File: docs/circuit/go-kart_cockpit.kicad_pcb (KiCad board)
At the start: 2 copper layers, 103.5 x 57.2 mm, 36 parts, among them P1 Power, Q1 TIP120, X1 Taster rechts (male), X10 Display (male), X11 PD7, X14 AVR-ISP-10, X15 Taster links (male), X16 Start/Stop/Rückwärts, X17 SDA PG4, X2 5V GND, X3 24V Hupe, X4 SCL, X5 CS, X6 PB6, X7 J5, X8 J3, X9 Bluetooth-Modul

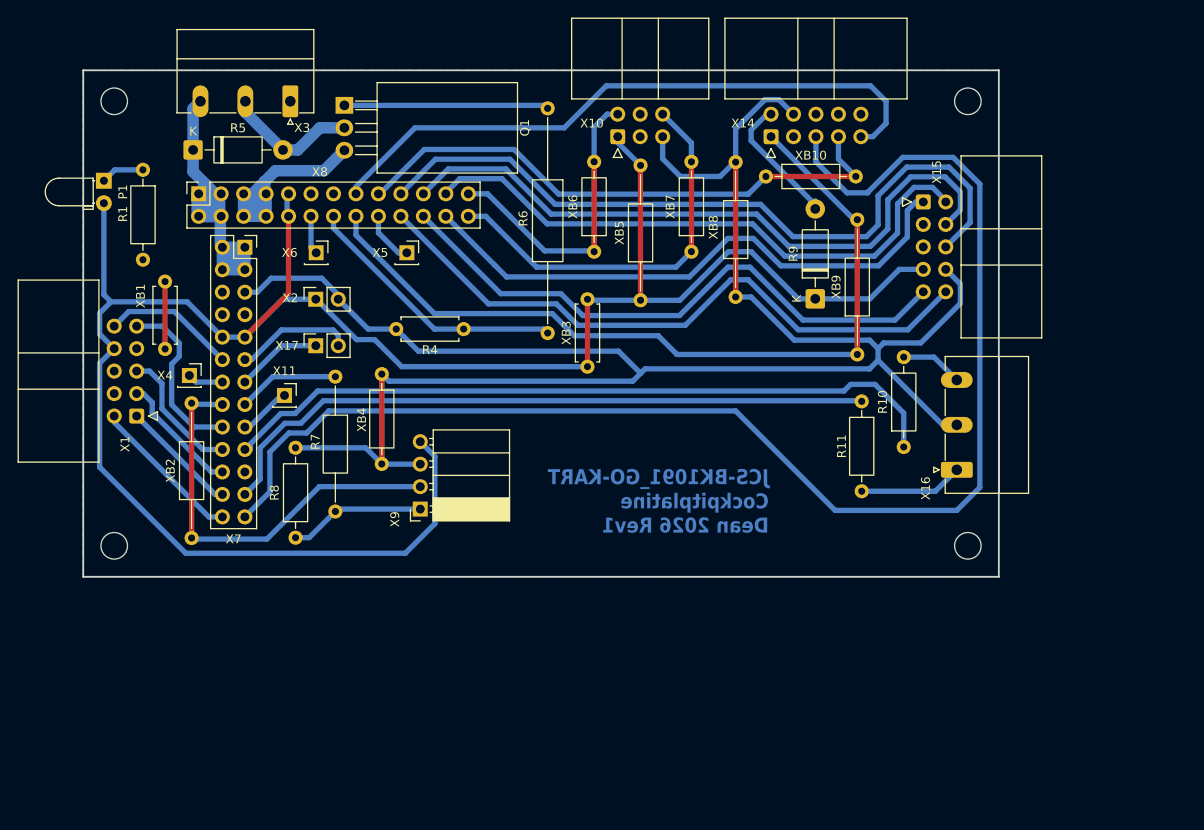
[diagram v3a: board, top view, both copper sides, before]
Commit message: feat(PCB): replace TIP120 with MOSFET
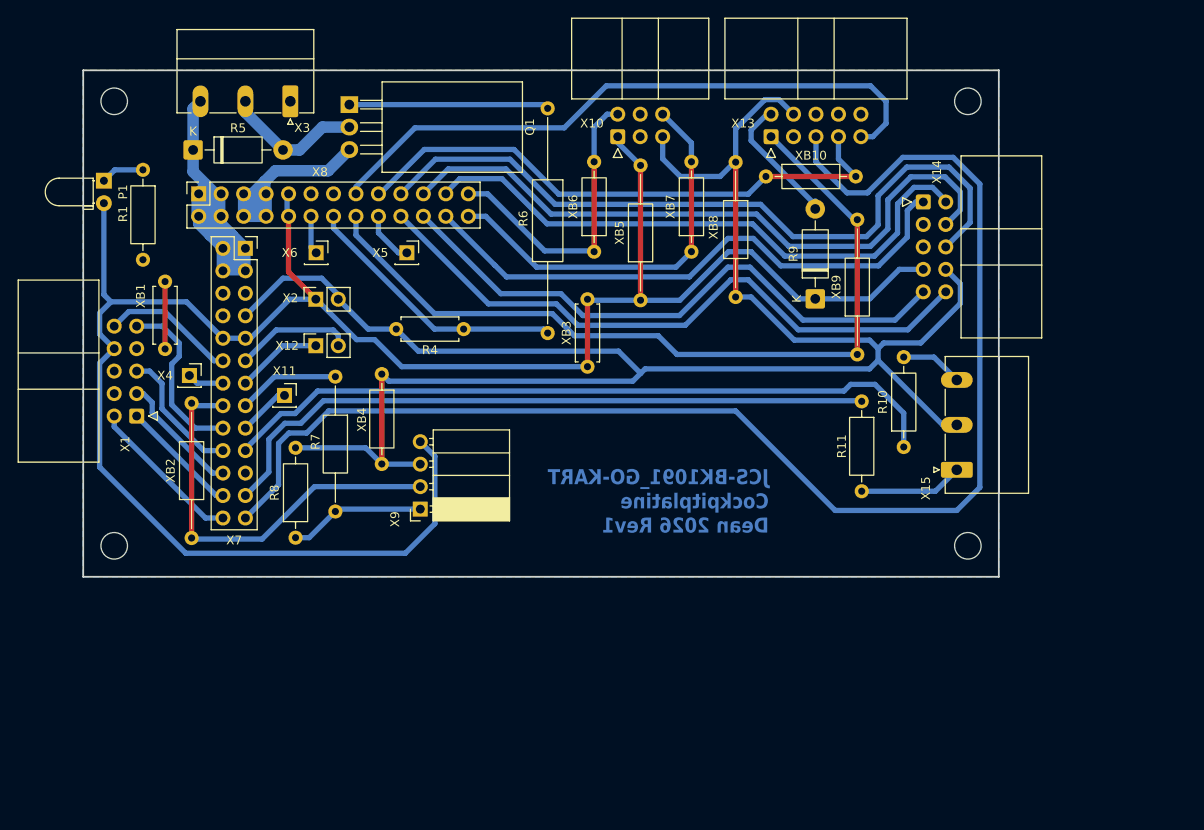
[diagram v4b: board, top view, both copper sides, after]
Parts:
- Q1: value TIP120 -> IRLIZ44N
- R6: value 470 -> 100
- moved Q1 0.57 mm to (69.2, 32.0)
- moved X7 0.14 mm to (57.5, 48.2)
- renumbered X17 to X12, X14 to X13, X15 to X14, X16 to X15
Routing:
- net +24V: track 54.1 -> 69.4 mm
- net Vcc (5V): track 236.5 -> 231.5 mm
- net GND: track 260.2 -> 261.8 mm
- net Net-(Q1-G): track 23.3 -> 22.6 mm
- net /Hupe (-): track 15.2 -> 15.8 mm
- net /PD7: track 5.96 -> 6.49 mm

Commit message: feat: rework of PCB, fix wrong connection
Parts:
- removed R10: 100, Resistor_THT:R_Axial_DIN0207_L6.3mm_D2.5mm_P10.16mm_Horizontal
- removed the R7 at (67.7, 62.8)
- removed R8: 5.6k, Resistor_THT:R_Axial_DIN0207_L6.3mm_D2.5mm_P10.16mm_Horizontal
- removed the X11 at (61.9, 64.9)
- removed the X2 at (65.5, 54.0)
- removed the X6 at (65.5, 48.8)
- added R2: 100, Resistor_THT:R_Axial_DIN0207_L6.3mm_D2.5mm_P10.16mm_Horizontal, F.Cu at (71.8, 59.5)
- added R3: 820, Resistor_THT:R_Axial_DIN0309_L9.0mm_D3.2mm_P12.70mm_Horizontal, F.Cu at (121.0, 44.9)
- added R5: 5.6k, Resistor_THT:R_Axial_DIN0207_L6.3mm_D2.5mm_P10.16mm_Horizontal, F.Cu at (79.2, 95.2)
- added X10: CS, Connector_PinSocket_2.54mm:PinSocket_1x01_P2.54mm_Vertical, F.Cu at (76.2, 70.2)
- added X7: PD1 PG4 VCC GND, Connector_PinSocket_2.54mm:PinSocket_1x04_P2.54mm_Vertical, F.Cu at (62.2, 85.4)
- added XB11: MISO, TestPoint:TestPoint_2Pads_Pitch5.08mm_Drill1.3mm, F.Cu at (127.2, 100.1)
- added XB12: /RESET, Resistor_THT:R_Axial_DIN0207_L6.3mm_D2.5mm_P15.24mm_Horizontal, F.Cu at (95.6, 95.0)
- Q1: value IRLIZ44N -> IRL3803; footprint Library:TO-220-3_Horizontal_TabDown_no_hole -> Package_TO_SOT_THT:TO-220F-3_Horizontal_TabDown
- R1: value 820 -> 100
- R11: value 100 -> 10k; footprint Resistor_THT:R_Axial_DIN0207_L6.3mm_D2.5mm_P10.16mm_Horizontal -> Resistor_THT:R_Axial_DIN0207_L6.3mm_D2.5mm_P7.62mm_Horizontal
- R4: value 10k -> 3.3k; footprint Resistor_THT:R_Axial_DIN0207_L6.3mm_D2.5mm_P7.62mm_Horizontal -> Resistor_THT:R_Axial_DIN0207_L6.3mm_D2.5mm_P10.16mm_Horizontal
- R6: value 100 -> 1N5817; footprint Resistor_THT:R_Axial_DIN0309_L9.0mm_D3.2mm_P25.40mm_Horizontal -> Diode_THT:D_DO-41_SOD81_P10.16mm_Horizontal
- R9: value 1N5817 -> 100; footprint Diode_THT:D_DO-41_SOD81_P10.16mm_Horizontal -> Resistor_THT:R_Axial_DIN0207_L6.3mm_D2.5mm_P7.62mm_Horizontal
- X12: value SDA PG4 -> PB6; footprint Connector_PinSocket_2.54mm:PinSocket_1x02_P2.54mm_Vertical -> Connector_PinSocket_2.54mm:PinSocket_1x01_P2.54mm_Vertical
- X4: value SCL -> PC2 PG1 PD7; footprint Connector_PinSocket_2.54mm:PinSocket_1x01_P2.54mm_Vertical -> Connector_PinSocket_2.54mm:PinSocket_1x03_P2.54mm_Vertical
- X5: value CS -> SCL
- XB1: footprint Resistor_THT:R_Axial_DIN0207_L6.3mm_D2.5mm_P7.62mm_Horizontal -> Resistor_THT:R_Axial_DIN0207_L6.3mm_D2.5mm_P10.16mm_Horizontal
- XB10: value ISP_SCK -> TXD0
- XB2: value ~ -> Vcc; footprint Resistor_THT:R_Axial_DIN0207_L6.3mm_D2.5mm_P15.24mm_Horizontal -> Resistor_THT:R_Axial_DIN0207_L6.3mm_D2.5mm_P10.16mm_Horizontal
- XB3: value Display_Vcc -> Vcc; footprint Resistor_THT:R_Axial_DIN0207_L6.3mm_D2.5mm_P7.62mm_Horizontal -> Resistor_THT:R_Axial_DIN0207_L6.3mm_D2.5mm_P10.16mm_Horizontal
- XB4: value Display_GND -> Vcc; footprint Resistor_THT:R_Axial_DIN0207_L6.3mm_D2.5mm_P10.16mm_Horizontal -> Resistor_THT:R_Axial_DIN0207_L6.3mm_D2.5mm_P7.62mm_Horizontal
- XB5: value Display_Vcc -> GND
- XB6: value TXD0 -> GND
- XB7: value RXD0 -> GND; footprint Resistor_THT:R_Axial_DIN0207_L6.3mm_D2.5mm_P10.16mm_Horizontal -> Resistor_THT:R_Axial_DIN0207_L6.3mm_D2.5mm_P7.62mm_Horizontal
- XB8: value GND -> ~
- XB9: value ISP_MOSI -> RXD0; footprint Resistor_THT:R_Axial_DIN0207_L6.3mm_D2.5mm_P15.24mm_Horizontal -> Resistor_THT:R_Axial_DIN0207_L6.3mm_D2.5mm_P10.16mm_Horizontal
- moved XB8 89.0 mm to (52.5, 103.9), turned to 90 degrees
- moved P1 85.5 mm to (126.8, 46.6), turned to 180 degrees
- moved X14 79.3 mm to (95.3, 103.9), turned to 0 degrees
- moved R7 75.7 mm to (95.4, 98.9)
- moved Q1 74.8 mm to (122.3, 84.8), turned to 180 degrees
- moved X1 73.8 mm to (69.5, 45.4), turned to 180 degrees
- moved R11 55.7 mm to (72.1, 73.5), turned to 180 degrees
- moved XB4 53.5 mm to (126.2, 58.0), turned to 90 degrees
- moved R6 43.9 mm to (124.2, 61.9)
- moved X13 43.4 mm to (129.2, 77.2), turned to 0 degrees
- moved X5 42.6 mm to (52.2, 84.2)
- moved R4 41.2 mm to (66.0, 95.2), turned to 0 degrees
- moved X2 39.5 mm to (81.4, 51.3), turned to 90 degrees
- moved X9 38.6 mm to (129.2, 60.4), turned to 0 degrees
- moved X4 36.0 mm to (62.2, 96.8), turned to 180 degrees
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- renumbered R5 to R7, X15 to X1, X8 to X11, X3 to X14, X1 to X2, X14 to X3, X7 to X6, X9 to X8, X10 to X9
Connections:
- R1 pad 1: Net-(P1-K) -> /PB7_SW_Reverse
- R1 pad 2: GND -> Net-(X1-4)
- R11 pad 1: /PC2_SW_Start -> PB4_OC2A
- R11 pad 2: Net-(R11-Pad2) -> GND
- R4 pad 1: PB4_OC2A -> PD3_TXD1
- R4 pad 2: GND -> /BL_RX3V3
- R6 pad 1: Net-(Q1-G) -> Vcc (5V)
- R6 pad 2: PB4_OC2A -> Net-(R6-A)
- R9 pad 1: Vcc (5V) -> Net-(Q1-G)
- R9 pad 2: Net-(R9-A) -> PB4_OC2A
- X1 pad 1: Net-(R11-Pad2) -> Net-(R2-Pad2)
- X1 pad 3: Net-(X15-4) -> Net-(X1-4)
- X11 pad 11: unconnected-(X8-Pin_11-Pad11) -> /PB7_SW_Reverse
- X11 pad 13: unconnected-(X8-Pin_13-Pad13) -> /PB5_SW_Start
- X12 pad 1: /PD1_SDA -> /PB6_OC1B
- X13 pad 2: Net-(R9-A) -> Net-(R6-A)
- X14 pad 2: /Hupe (-) -> +24V
- X14 pad 3: +24V -> /Hupe (-)
- X4 pad 1: /PD0_SCL -> /PC2
- X5 pad 1: /PB0_CS -> /PD0_SCL
- X6 pad 19: /PG1_SW_Reverse -> /PG1
- X6 pad 23: /PC2_SW_Start -> /PC2
- X9 pad 2: PE1_TXD0 -> PE0_RXD0
- X9 pad 6: PE0_RXD0 -> PE1_TXD0
- XB10 pad 1: PB1_SCK -> PE1_TXD0
- XB10 pad 2: PB1_SCK -> PE1_TXD0
- XB2 pad 1: PD2_RXD1 -> Vcc (5V)
- XB2 pad 2: PD2_RXD1 -> Vcc (5V)
- XB4 pad 1: GND -> Vcc (5V)
- XB4 pad 2: GND -> Vcc (5V)
- XB5 pad 1: Vcc (5V) -> GND
- XB5 pad 2: Vcc (5V) -> GND
- XB6 pad 1: PE1_TXD0 -> GND
- XB6 pad 2: PE1_TXD0 -> GND
- XB7 pad 1: PE0_RXD0 -> GND
- XB7 pad 2: PE0_RXD0 -> GND
- XB8 pad 1: GND -> PD2_RXD1
- XB8 pad 2: GND -> PD2_RXD1
- XB9 pad 1: PB2_MOSI -> PE0_RXD0
- XB9 pad 2: PB2_MOSI -> PE0_RXD0
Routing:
- net /PG1_SW_Reverse: track 84.1 -> 0.00 mm
- net /PC2_SW_Start: track 76.3 -> 0.00 mm
- net PB1_SCK: track 64.3 -> 138.4 mm
- net PC0_SW_BlinkerR: track 13.5 -> 84.5 mm
- net PB3_MISO: track 72.1 -> 143.0 mm
- net PC3_LED_BlinkerR: track 17.8 -> 88.4 mm
- net PG2_SW_GearDown: track 14.2 -> 81.4 mm
- net PG0_SW_GearUp: track 15.1 -> 79.3 mm
- net PD4_LED_GearUp: track 19.8 -> 83.5 mm
- net PG3_LED_GearDown: track 15.3 -> 77.3 mm
- net +24V: track 69.4 -> 129.9 mm
- net Vcc (5V): track 231.5 -> 179.9 mm
- net GND: track 261.8 -> 305.9 mm
- net /RESET: track 156.6 -> 116.1 mm
- net PE7_SW_Warnblinker: track 83.5 -> 46.4 mm
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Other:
- board size 103.5 x 57.2 mm -> 96.8 x 66.2 mm
- board text added: "DSUB9-CAN"
- board text added: "JCS-BK1091_GO-KART Cockpitplatine Dean 2026 Rev2"
- board text added: "M2"
- board text removed: "JCS-BK1091_GO-KART Cockpitplatine Dean 2026 Rev1"

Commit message: feat(PCB): replace 100 ohm preresistors with 330
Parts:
- R1, R2: value 100 -> 330
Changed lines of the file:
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@@
 			)
 		)
-		(property "Value" "100"
+		(property "Value" "330"
 			(at 5.08 2.37 90)
 			(layer "F.Fab")
@@
 			)
 		)
-		(property "Value" "100"
+		(property "Value" "330"
 			(at 5.08 2.37 90)
 			(layer "F.Fab")
@@
 	)
 	(zone
-		(net 38)
-		(net_name "{slash}PB5_SW_Start")
-		(layer "B.Cu")
-		(name "$teardrop_padvia$")
-		(hatch none 0.1)
-		(priority 30125)
-		(attr
-			(teardrop
-				(type padvia)
-			)
-		)
-		(connect_pads yes
-			(clearance 0)
-		)
-		(min_thickness 0.0254)
-		(filled_areas_thickness no)
-		(fill yes
-			(thermal_gap 0.5)
-			(thermal_bridge_width 0.5)
-			(island_removal_mode 1)
-			(island_area_min 10)
-		)
-		(polygon
-			(pts
-				(xy 70.277304 60.548432) (xy 70.701568 60.972696) (xy 72.250013 60.248323) (xy 71.750707 59.499293)
-				(xy 71.001677 58.999987)
-			)
-		)
-	)
-	(zone
 		(net 11)
 		(net_name "{slash}RESET")
@@
 	)
 	(zone
-		(net 40)
-		(net_name "Net-(X1-4)")
-		(layer "B.Cu")
-		(name "$teardrop_padvia$")
-		(hatch none 0.1)
-		(priority 30140)
-		(attr
-			(teardrop
-				(type padvia)
-			)
-		)
-		(connect_pads yes
-			(clearance 0)
-		)
-		(min_thickness 0.0254)
-		(filled_areas_thickness no)
-		(fill yes
-			(thermal_gap 0.5)
-			(thermal_bridge_width 0.5)
-			(island_removal_mode 1)
-			(island_area_min 10)
-		)
-		(polygon
-			(pts
-				(xy 58.60693 48.067334) (xy 58.182666 47.64307) (xy 56.999987 48.591677) (xy 57.499293 49.340707)
-				(xy 58.382707 49.515581)
-			)
-		)
-	)
-	(zone
 		(net 4)
 		(net_name "+24V")
@@
 	)
 	(zone
+		(net 41)
+		(net_name "Net-(R2-Pad2)")
+		(layer "B.Cu")
+		(name "$teardrop_padvia$")
+		(hatch none 0.1)
+		(priority 30004)
+		(attr
+			(teardrop
+				(type padvia)
+			)
+		)
+		(connect_pads yes
+			(clearance 0)
+		)
+		(min_thickness 0.0254)
+		(filled_areas_thickness no)
+		(fill yes
+			(thermal_gap 0.5)
+			(thermal_bridge_width 0.5)
+			(island_removal_mode 1)
+			(island_area_min 10)
+		)
+		(polygon
+			(pts
+				(xy 71.067334 47.64307) (xy 70.64307 48.067334) (xy 70.867293 49.515581) (xy 71.750707 49.340707)
+				(xy 72.250013 48.591677)
+			)
+		)
+	)
+	(zone
 		(net 22)
 		(net_name "PE3_SW_BlinkerL")
@@
 	)
 	(zone
-		(net 4)
-		(net_name "+24V")
+		(net 1)
+		(net_name "/Hupe (-)")
 		(layer "B.Cu")
 		(name "$teardrop_padvia$")
 		(hatch none 0.1)
-		(priority 30033)
+		(priority 30000)
 		(attr
 			(teardrop
@@
 		(polygon
 			(pts
-				(xy 55.239056 68.406909) (xy 54.319817 69.326148) (xy 55.291677 70.627105) (xy 56.040707 70.127799)
-				(xy 56.540013 69.378769)
+				(xy 119.1 86.704198) (xy 120.4 86.704198) (xy 120.684198 85.003324) (xy 119.75 84.769) (xy 118.815802 85.003324)
 			)
 		)
 	)
 	(zone
-		(net 37)
-		(net_name "{slash}PB7_SW_Reverse")
+		(net 4)
+		(net_name "+24V")
 		(layer "B.Cu")
 		(name "$teardrop_padvia$")
 		(hatch none 0.1)
-		(priority 30129)
+		(priority 30033)
 		(attr
 			(teardrop
@@
 		(polygon
 			(pts
-				(xy 58.972696 58.451568) (xy 58.548432 58.027304) (xy 56.999987 58.751677) (xy 57.499293 59.500707)
-				(xy 58.248323 60.000013)
+				(xy 55.239056 68.406909) (xy 54.319817 69.326148) (xy 55.291677 70.627105) (xy 56.040707 70.127799)
+				(xy 56.540013 69.378769)
 			)
 		)
@@
 	)
 	(zone
+		(net 40)
+		(net_name "Net-(X1-4)")
+		(layer "B.Cu")
+		(name "$teardrop_padvia$")
+		(hatch none 0.1)
+		(priority 30003)
+		(attr
+			(teardrop
+				(type padvia)
+			)
+		)
+		(connect_pads yes
+			(clearance 0)
+		)
+		(min_thickness 0.0254)
+		(filled_areas_thickness no)
+		(fill yes
+			(thermal_gap 0.5)
+			(thermal_bridge_width 0.5)
+			(island_removal_mode 1)
+			(island_area_min 10)
+		)
+		(polygon
+			(pts
+				(xy 58.60693 48.067334) (xy 58.182666 47.64307) (xy 56.999987 48.591677) (xy 57.499293 49.340707)
+				(xy 58.382707 49.515581)
+			)
+		)
+	)
+	(zone
 		(net 31)
 		(net_name "/PB6_OC1B")
@@
 	)
 	(zone
-		(net 3)
-		(net_name "Net-(Q1-G)")
+		(net 5)
+		(net_name "Vcc (5V)")
 		(layer "B.Cu")
 		(name "$teardrop_padvia$")
 		(hatch none 0.1)
-		(priority 30144)
+		(priority 30137)
 		(attr
 			(teardrop
@@
 		(polygon
 			(pts
-				(xy 121.906309 82.732045) (xy 121.482045 83.156309) (xy 121.3375 83.77) (xy 122.290707 84.770707)
-				(xy 122.965895 83.77)
+				(xy 127.971091 59.296828) (xy 127.546828 59.721091) (xy 128.36 60.890163) (xy 129.210707 60.420707)
+				(xy 129.454361 59.57)
 			)
 		)
 	)
 	(zone
-		(net 5)
-		(net_name "Vcc (5V)")
+		(net 14)
+		(net_name "/PD1_SDA")
 		(layer "B.Cu")
 		(name "$teardrop_padvia$")
 		(hatch none 0.1)
-		(priority 30137)
+		(priority 30065)
 		(attr
 			(teardrop
@@
 		(polygon
 			(pts
-				(xy 127.971091 59.296828) (xy 127.546828 59.721091) (xy 128.36 60.890163) (xy 129.210707 60.420707)
-				(xy 129.454361 59.57)
+				(xy 60.25 85.067092) (xy 60.25 85.667092) (xy 61.25 86.368546) (xy 62.251 85.37) (xy 61.25 84.37)
 			)
 		)
 	)
 	(zone
-		(net 14)
-		(net_name "/PD1_SDA")
+		(net 9)
+		(net_name "PE0_RXD0")
 		(layer "B.Cu")
 		(name "$teardrop_padvia$")
 		(hatch none 0.1)
-		(priority 30065)
+		(priority 30136)
 		(attr
 			(teardrop
@@
 		(polygon
 			(pts
-				(xy 60.25 85.067092) (xy 60.25 85.667092) (xy 61.25 86.368546) (xy 62.251 85.37) (xy 61.25 84.37)
+				(xy 132.7284 61.822664) (xy 133.152664 61.3984) (xy 132.456749 59.947765) (xy 131.749293 60.419293)
+				(xy 131.277765 61.126749)
 			)
 		)
 	)
 	(zone
-		(net 9)
-		(net_name "PE0_RXD0")
+		(net 32)
+		(net_name "/PD7")
 		(layer "B.Cu")
 		(name "$teardrop_padvia$")
 		(hatch none 0.1)
-		(priority 30136)
+		(priority 30145)
 		(attr
 			(teardrop
@@
 		(polygon
 			(pts
-				(xy 132.7284 61.822664) (xy 133.152664 61.3984) (xy 132.456749 59.947765) (xy 131.749293 60.419293)
-				(xy 131.277765 61.126749)
+				(xy 60.028844 90.953108) (xy 60.453108 90.528844) (xy 59.080013 89.698769) (xy 58.579293 90.446385)
+				(xy 58.755581 91.329799)
 			)
 		)
 	)
 	(zone
-		(net 32)
-		(net_name "/PD7")
+		(net 37)
+		(net_name "{slash}PB7_SW_Reverse")
 		(layer "B.Cu")
 		(name "$teardrop_padvia$")
 		(hatch none 0.1)
-		(priority 30145)
+		(priority 30001)
 		(attr
 			(teardrop
@@
 		(polygon
 			(pts
-				(xy 60.028844 90.953108) (xy 60.453108 90.528844) (xy 59.080013 89.698769) (xy 58.579293 90.446385)
-				(xy 58.755581 91.329799)
+				(xy 58.972696 58.451568) (xy 58.548432 58.027304) (xy 56.999987 58.751677) (xy 57.499293 59.500707)
+				(xy 58.248323 60.000013)
 			)
 		)
@@
 	)
 	(zone
+		(net 3)
+		(net_name "Net-(Q1-G)")
+		(layer "B.Cu")
+		(name "$teardrop_padvia$")
+		(hatch none 0.1)
+		(priority 30005)
+		(attr
+			(teardrop
+				(type padvia)
+			)
+		)
+		(connect_pads yes
+			(clearance 0)
+		)
+		(min_thickness 0.0254)
+		(filled_areas_thickness no)
+		(fill yes
+			(thermal_gap 0.5)
+			(thermal_bridge_width 0.5)
+			(island_removal_mode 1)
+			(island_area_min 10)
+		)
+		(polygon
+			(pts
+				(xy 121.906309 82.732045) (xy 121.482045 83.156309) (xy 121.3375 83.77) (xy 122.290707 84.770707)
+				(xy 122.965895 83.77)
+			)
+		)
+	)
+	(zone
 		(net 6)
 		(net_name "PD3_TXD1")
@@
 	)
 	(zone
+		(net 38)
+		(net_name "{slash}PB5_SW_Start")
+		(layer "B.Cu")
+		(name "$teardrop_padvia$")
+		(hatch none 0.1)
+		(priority 30002)
+		(attr
+			(teardrop
+				(type padvia)
+			)
+		)
+		(connect_pads yes
+			(clearance 0)
+		)
+		(min_thickness 0.0254)
+		(filled_areas_thickness no)
+		(fill yes
+			(thermal_gap 0.5)
+			(thermal_bridge_width 0.5)
+			(island_removal_mode 1)
+			(island_area_min 10)
+		)
+		(polygon
+			(pts
+				(xy 70.277304 60.548432) (xy 70.701568 60.972696) (xy 72.250013 60.248323) (xy 71.750707 59.499293)
+				(xy 71.001677 58.999987)
+			)
+		)
+	)
+	(zone
 		(net 4)
 		(net_name "+24V")
@@
 	)
 	(zone
-		(net 1)
-		(net_name "/Hupe (-)")
-		(layer "B.Cu")
-		(name "$teardrop_padvia$")
-		(hatch none 0.1)
-		(priority 30011)
-		(attr
-			(teardrop
-				(type padvia)
-			)
-		)
-		(connect_pads yes
-			(clearance 0)
-		)
-		(min_thickness 0.0254)
-		(filled_areas_thickness no)
-		(fill yes
-			(thermal_gap 0.5)
-			(thermal_bridge_width 0.5)
-			(island_removal_mode 1)
-			(island_area_min 10)
-		)
-		(polygon
-			(pts
-				(xy 119.1 86.704198) (xy 120.4 86.704198) (xy 120.684198 85.003324) (xy 119.75 84.769) (xy 118.815802 85.003324)
-			)
-		)
-	)
-	(zone
 		(net 9)
 		(net_name "PE0_RXD0")
@@
 			)
 		)
-	)
-	(zone
-		(net 41)
-		(net_name "Net-(R2-Pad2)")
-		(layer "B.Cu")
-		(name "$teardrop_padvia$")
-		(hatch none 0.1)
-		(priority 30139)
-		(attr
-			(teardrop
-				(type padvia)
-			)
-		)
-		(connect_pads yes
-			(clearance 0)
-		)
-		(min_thickness 0.0254)
-		(filled_areas_thickness no)
-		(fill yes
-			(thermal_gap 0.5)
-			(thermal_bridge_width 0.5)
-			(island_removal_mode 1)
-			(island_area_min 10)
-		)
-		(polygon
-			(pts
-				(xy 71.067334 47.64307) (xy 70.64307 48.067334) (xy 70.867293 49.515581) (xy 71.750707 49.340707)
-				(xy 72.250013 48.591677)
-			)
-		)
